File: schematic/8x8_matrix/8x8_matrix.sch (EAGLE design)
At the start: 69 parts, among them U1 ATTINY85-20PU

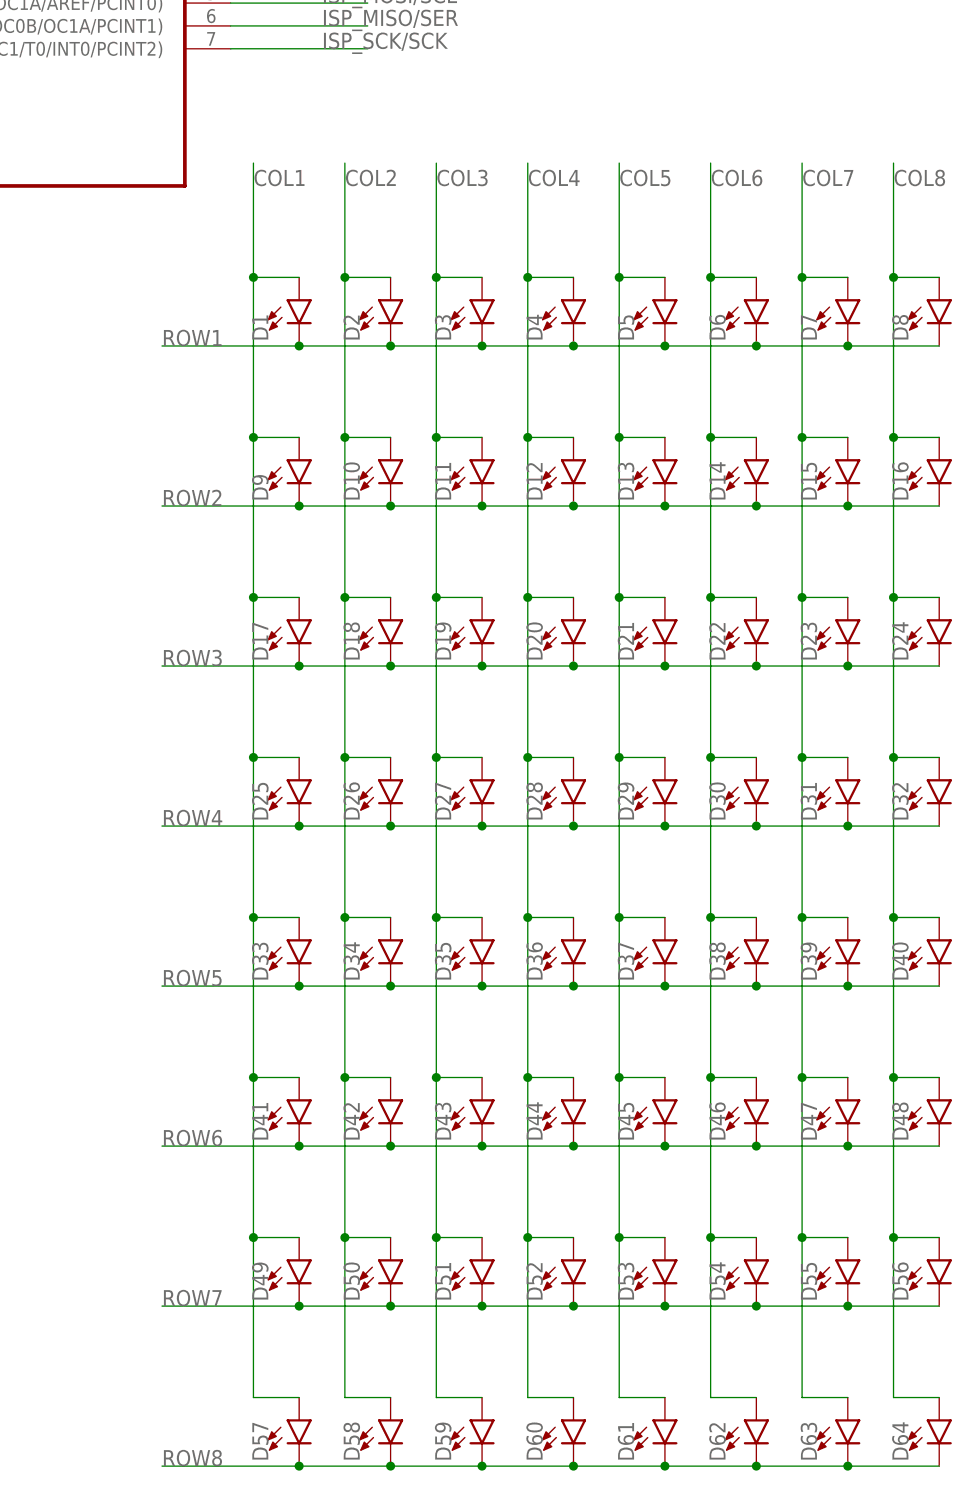
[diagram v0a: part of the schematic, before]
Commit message: _Serial now reads and writes bytes instead of data_packet
The work of assembling data_packet is now in the main loop instead of in _Serial
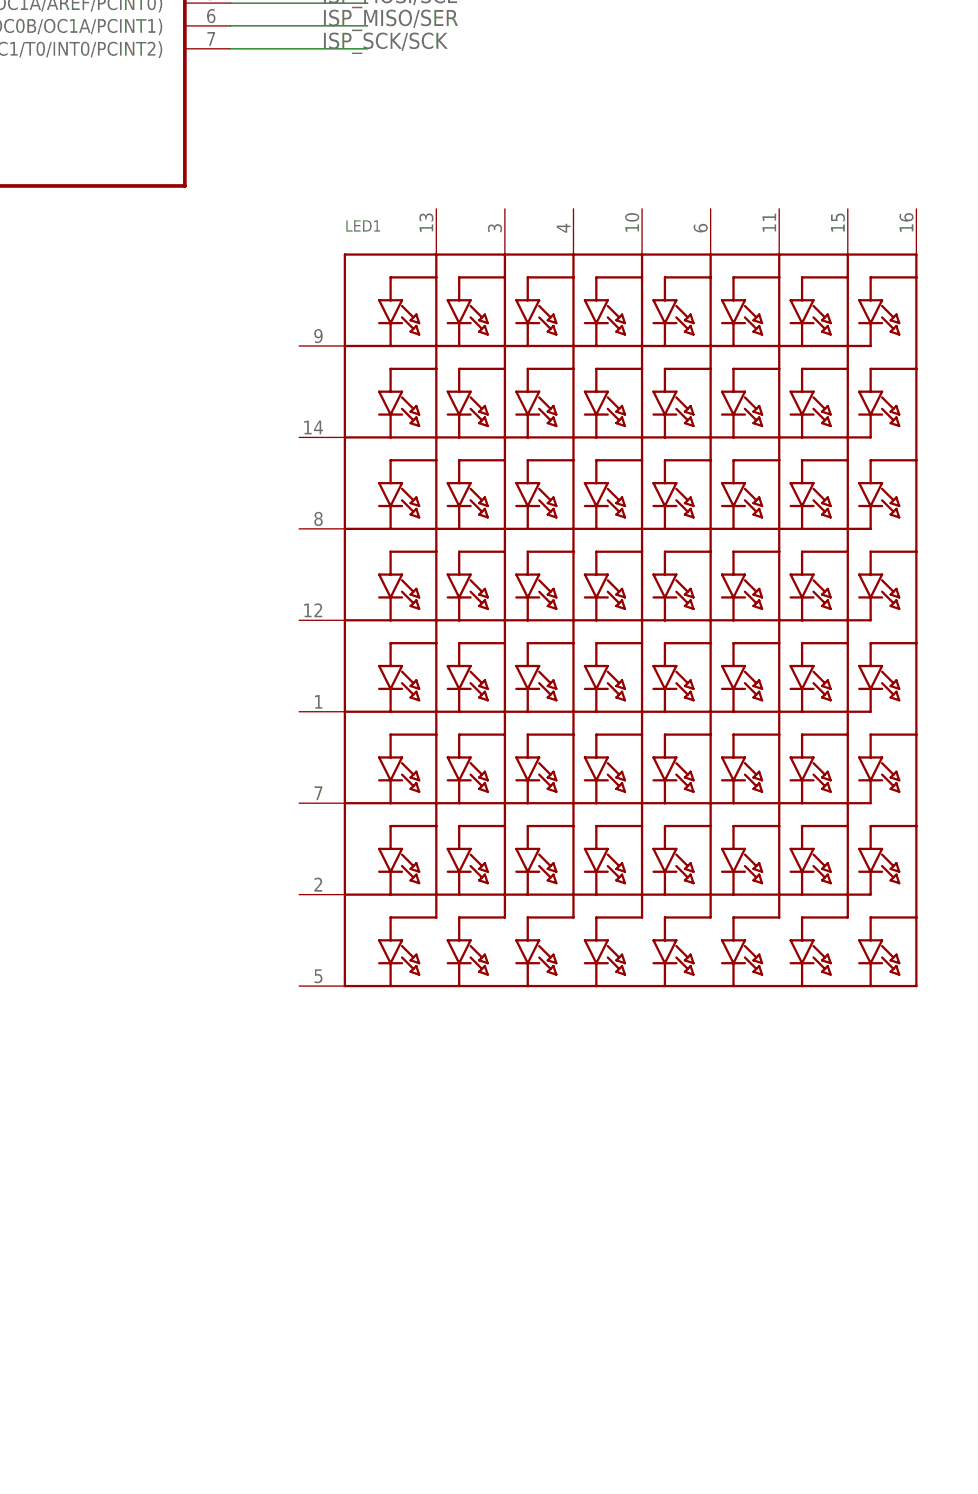
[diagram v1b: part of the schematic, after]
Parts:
- removed D1, D10, D11, D12, D13, D14, D15, D16, D17, D18, D19, D2, D20, D21, D22, D23, D24, D25, D26, D27, D28, D29, D3, D30, D31, D32, D33, D34, D35, D36, D37, D38, D39, D4, D40, D41, D42, D43, D44, D45, D46, D47, D48, D49, D5, D50, D51, D52, D53, D54, D55, D56, D57, D58, D59, D6, D60, D61, D62, D63, D64, D7, D8, D9: (no value), SparkFun-LED:LED5MM-KIT
- added LED1: (no value), adafruit:SEGMENT_8X8_ROWCATHODEM12A881UR
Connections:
- net COL1: no longer D1.A, D17.A, D25.A, D33.A, D41.A, D49.A, D57.A, D9.A
- net COL2: no longer D10.A, D18.A, D2.A, D26.A, D34.A, D42.A, D50.A, D58.A
- net COL3: no longer D11.A, D19.A, D27.A, D3.A, D35.A, D43.A, D51.A, D59.A
- net COL4: no longer D12.A, D20.A, D28.A, D36.A, D4.A, D44.A, D52.A, D60.A
- net COL5: no longer D13.A, D21.A, D29.A, D37.A, D45.A, D5.A, D53.A, D61.A
- net COL6: no longer D14.A, D22.A, D30.A, D38.A, D46.A, D54.A, D6.A, D62.A
- net COL7: no longer D15.A, D23.A, D31.A, D39.A, D47.A, D55.A, D63.A, D7.A
- net COL8: no longer D16.A, D24.A, D32.A, D40.A, D48.A, D56.A, D64.A, D8.A
- net ROW1: no longer D1.C, D2.C, D3.C, D4.C, D5.C, D6.C, D7.C, D8.C
- net ROW2: no longer D10.C, D11.C, D12.C, D13.C, D14.C, D15.C, D16.C, D9.C
- net ROW3: no longer D17.C, D18.C, D19.C, D20.C, D21.C, D22.C, D23.C, D24.C
- net ROW4: no longer D25.C, D26.C, D27.C, D28.C, D29.C, D30.C, D31.C, D32.C
- net ROW5: no longer D33.C, D34.C, D35.C, D36.C, D37.C, D38.C, D39.C, D40.C
- net ROW6: no longer D41.C, D42.C, D43.C, D44.C, D45.C, D46.C, D47.C, D48.C
- net ROW7: no longer D49.C, D50.C, D51.C, D52.C, D53.C, D54.C, D55.C, D56.C
- net ROW8: no longer D57.C, D58.C, D59.C, D60.C, D61.C, D62.C, D63.C, D64.C
